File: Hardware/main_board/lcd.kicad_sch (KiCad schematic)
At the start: 0 parts

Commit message: sch: done LCD
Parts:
- added C66: 2.2uF, symbol Device:C
- added C67, C68, C69, C70: TBD, symbol Device:C
- added C71, C73, C74: TBD, symbol Device:C_Small
- added C72: 2.2uF, symbol Device:C_Small
- added C75: 100nF, symbol Device:C
- added C76: 100pF, symbol Device:C
- added J2: LCD, symbol Connector_Generic_MountingPin:Conn_01x30_MountingPin
- added J3: BACK_LIGHT, symbol Connector_Generic:Conn_01x02
- added R18: 0R, symbol Device:R_US
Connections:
- new net: C69.2, J2.24 (Pin_24)
- new net: C72.2, C73.1, J2.19 (Pin_19)
- new net: C73.2, J2.18 (Pin_18)
- new net: C67.2, J2.26 (Pin_26)
- new net: C68.2, J2.25 (Pin_25)
- new net: J3.1 (Pin_1), R18.1
- new net: C72.1, J2.20 (Pin_20)
- new net: C74.2, J2.17 (Pin_17)
- new net: C71.2, J2.21 (Pin_21)
- new net: C71.1, J2.22 (Pin_22)
- new net: C70.2, J2.23 (Pin_23)
- new net: C66.2, J2.27 (Pin_27)
- new net +3.3V: C75.2, C76.2, J2.10 (Pin_10), J2.11 (Pin_11), J2.12 (Pin_12), J2.15 (Pin_15), J2.5 (Pin_5), J2.6 (Pin_6), J2.7 (Pin_7), J2.8 (Pin_8), J2.9 (Pin_9)
- new net DISPLAY_CS: J2.2 (Pin_2)
- new net DISPLAY_DI: J2.4 (Pin_4)
- new net DISPLAY_RST: J2.3 (Pin_3)
- new net GND: C66.1, C67.1, C68.1, C69.1, C70.1, C74.1, C75.1, C76.1, J2.16 (Pin_16), J2.28 (Pin_28), J2.29 (Pin_29), J2.MP (MountPin)
- new net LCD_LED: J3.2 (Pin_2)
- new net SPI_D_MOSI: J2.14 (Pin_14)
- new net SPI_D_SCK: J2.13 (Pin_13)
- new net VSYS: R18.2
- no-connect marks 0 -> 2
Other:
- note added: "BACK LIGHT"
- note added: "LCD"
- note added: "VDD"

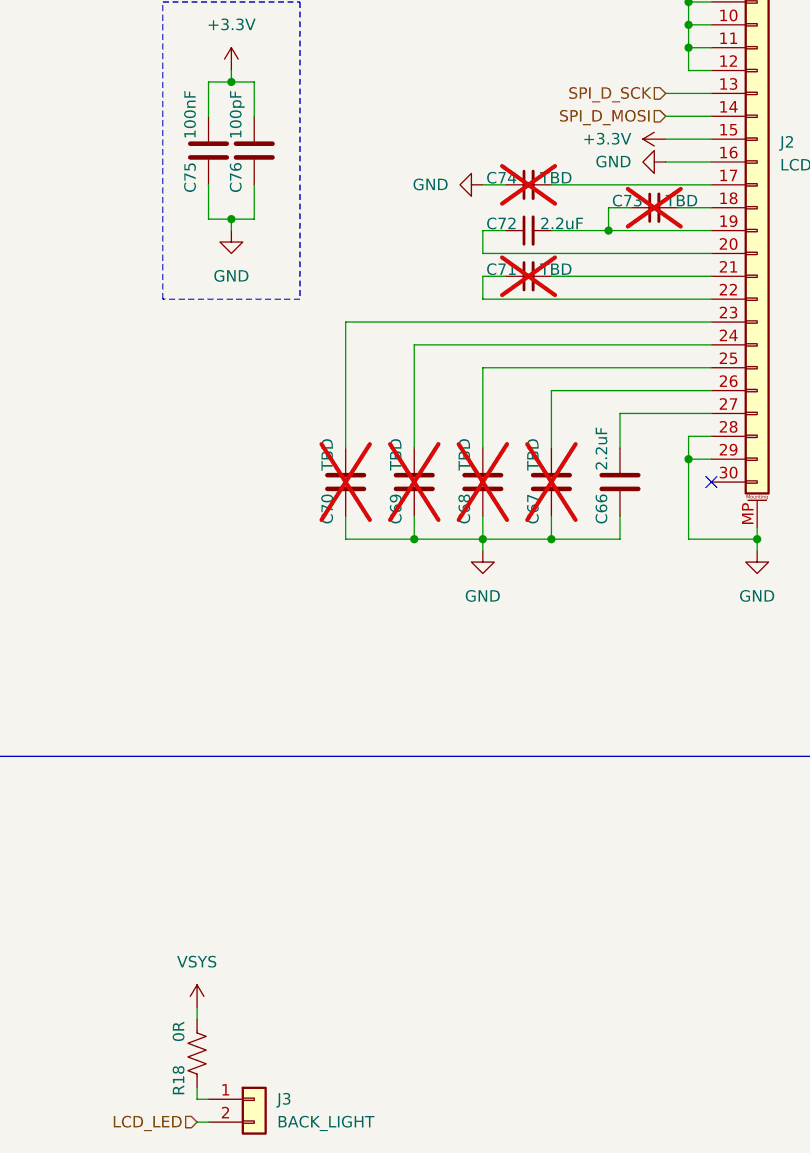
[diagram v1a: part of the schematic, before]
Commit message: sch: add some part of footprints
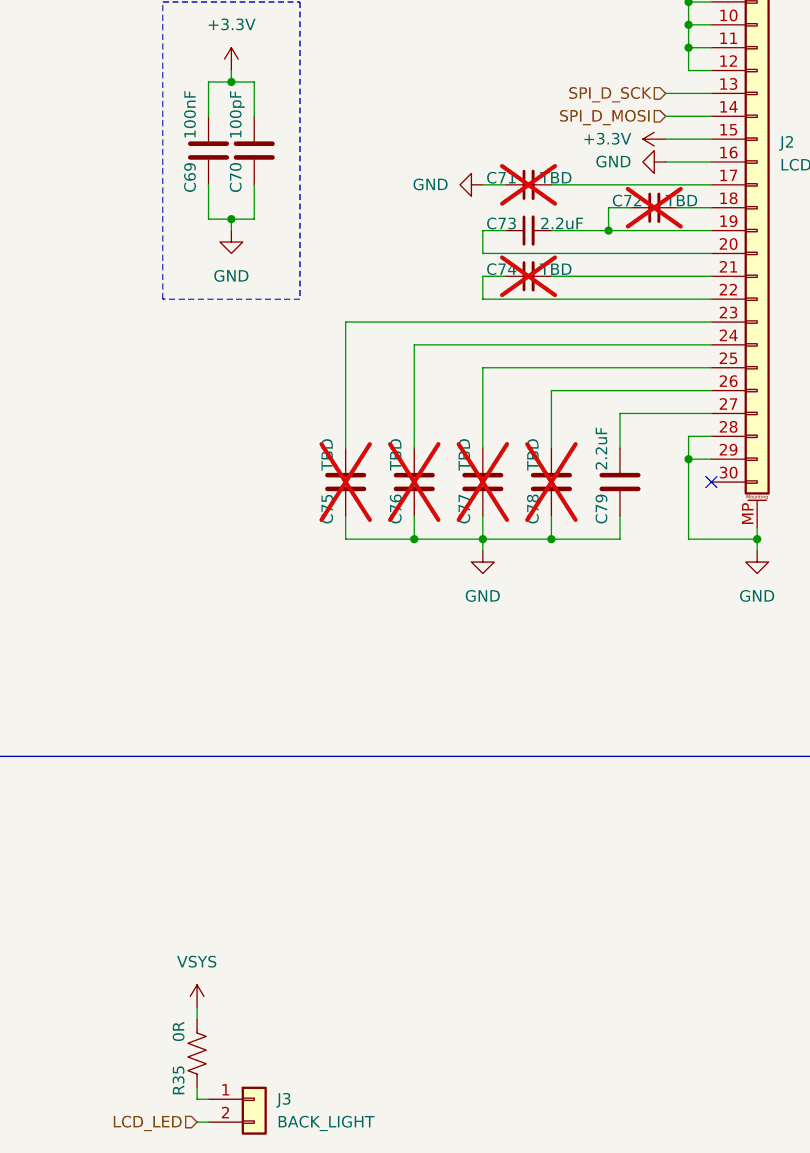
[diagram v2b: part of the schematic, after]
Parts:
- C69: renamed from C75; footprint (none) -> Capacitor_SMD:C_0402_1005Metric
- C70: renamed from C76; footprint (none) -> Capacitor_SMD:C_0402_1005Metric
- C71: renamed from C74; footprint (none) -> Capacitor_SMD:C_0402_1005Metric
- C72: renamed from C73; footprint (none) -> Capacitor_SMD:C_0402_1005Metric
- C73: renamed from C72; footprint (none) -> Capacitor_SMD:C_0402_1005Metric
- C74: renamed from C71; footprint (none) -> Capacitor_SMD:C_0402_1005Metric
- C75: renamed from C70; footprint (none) -> Capacitor_SMD:C_0402_1005Metric
- C76: renamed from C69; footprint (none) -> Capacitor_SMD:C_0402_1005Metric
- C77: renamed from C68; footprint (none) -> Capacitor_SMD:C_0402_1005Metric
- C78: renamed from C67; footprint (none) -> Capacitor_SMD:C_0402_1005Metric
- C79: renamed from C66; footprint (none) -> Capacitor_SMD:C_0402_1005Metric
- R35: renamed from R18; footprint (none) -> Resistor_SMD:R_0402_1005Metric
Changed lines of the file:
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@@
 		(on_board yes)
 		(dnp no)
-		(property "Reference" "C75"
+		(property "Reference" "C69"
 			(at 92.71 67.31 90)
 			(effects
@@
 			)
 		)
-		(property "Footprint" ""
+		(property "Footprint" "Capacitor_SMD:C_0402_1005Metric"
 			(at 93.0148 62.23 0)
 			(effects
@@
 			(project "main_board"
 				(path "/16216a68-6dea-41d7-8e15-2cc84f72f8e2/235dc31c-3814-4a70-a75b-2b905e486f6f"
-					(reference "C75")
+					(reference "C69")
 					(unit 1)
 				)
@@
 		(on_board yes)
 		(dnp yes)
-		(property "Reference" "C69"
+		(property "Reference" "C76"
 			(at 115.57 104.14 90)
 			(effects
@@
 			)
 		)
-		(property "Footprint" ""
+		(property "Footprint" "Capacitor_SMD:C_0402_1005Metric"
 			(at 115.8748 99.06 0)
 			(effects
@@
 			(project "main_board"
 				(path "/16216a68-6dea-41d7-8e15-2cc84f72f8e2/235dc31c-3814-4a70-a75b-2b905e486f6f"
-					(reference "C69")
+					(reference "C76")
 					(unit 1)
 				)
@@
 		(on_board yes)
 		(dnp yes)
-		(property "Reference" "C73"
+		(property "Reference" "C72"
 			(at 142.24 72.39 90)
 			(effects
@@
 			)
 		)
-		(property "Footprint" ""
+		(property "Footprint" "Capacitor_SMD:C_0402_1005Metric"
 			(at 143.51 72.39 0)
 			(effects
@@
 			(project "main_board"
 				(path "/16216a68-6dea-41d7-8e15-2cc84f72f8e2/235dc31c-3814-4a70-a75b-2b905e486f6f"
-					(reference "C73")
+					(reference "C72")
 					(unit 1)
 				)
@@
 		(on_board yes)
 		(dnp yes)
-		(property "Reference" "C67"
+		(property "Reference" "C78"
 			(at 130.81 104.14 90)
 			(effects
@@
 			)
 		)
-		(property "Footprint" ""
+		(property "Footprint" "Capacitor_SMD:C_0402_1005Metric"
 			(at 131.1148 99.06 0)
 			(effects
@@
 			(project "main_board"
 				(path "/16216a68-6dea-41d7-8e15-2cc84f72f8e2/235dc31c-3814-4a70-a75b-2b905e486f6f"
-					(reference "C67")
+					(reference "C78")
 					(unit 1)
 				)
@@
 		(on_board yes)
 		(dnp yes)
-		(property "Reference" "C68"
+		(property "Reference" "C77"
 			(at 123.19 104.14 90)
 			(effects
@@
 			)
 		)
-		(property "Footprint" ""
+		(property "Footprint" "Capacitor_SMD:C_0402_1005Metric"
 			(at 123.4948 99.06 0)
 			(effects
@@
 			(project "main_board"
 				(path "/16216a68-6dea-41d7-8e15-2cc84f72f8e2/235dc31c-3814-4a70-a75b-2b905e486f6f"
-					(reference "C68")
+					(reference "C77")
 					(unit 1)
 				)
@@
 		(dnp no)
 		(fields_autoplaced yes)
-		(property "Reference" "#PWR0108"
+		(property "Reference" "#PWR0115"
 			(at 96.52 81.28 0)
 			(effects
@@
 			(project "main_board"
 				(path "/16216a68-6dea-41d7-8e15-2cc84f72f8e2/235dc31c-3814-4a70-a75b-2b905e486f6f"
-					(reference "#PWR0108")
+					(reference "#PWR0115")
 					(unit 1)
 				)
@@
 		(on_board yes)
 		(dnp no)
-		(property "Reference" "R18"
+		(property "Reference" "R35"
 			(at 91.44 167.64 90)
 			(effects
@@
 			)
 		)
-		(property "Footprint" ""
+		(property "Footprint" "Resistor_SMD:R_0402_1005Metric"
 			(at 91.694 166.116 90)
 			(effects
@@
 			(project "main_board"
 				(path "/16216a68-6dea-41d7-8e15-2cc84f72f8e2/235dc31c-3814-4a70-a75b-2b905e486f6f"
-					(reference "R18")
+					(reference "R35")
 					(unit 1)
 				)
@@
 		(on_board yes)
 		(dnp no)
-		(property "Reference" "C72"
+		(property "Reference" "C73"
 			(at 128.27 74.93 90)
 			(effects
@@
 			)
 		)
-		(property "Footprint" ""
+		(property "Footprint" "Capacitor_SMD:C_0402_1005Metric"
 			(at 129.54 74.93 0)
 			(effects
@@
 			(project "main_board"
 				(path "/16216a68-6dea-41d7-8e15-2cc84f72f8e2/235dc31c-3814-4a70-a75b-2b905e486f6f"
-					(reference "C72")
+					(reference "C73")
 					(unit 1)
 				)
@@
 		(dnp no)
 		(fields_autoplaced yes)
-		(property "Reference" "#PWR0105"
+		(property "Reference" "#PWR0113"
 			(at 138.43 67.31 0)
 			(effects
@@
 			(project "main_board"
 				(path "/16216a68-6dea-41d7-8e15-2cc84f72f8e2/235dc31c-3814-4a70-a75b-2b905e486f6f"
-					(reference "#PWR0105")
+					(reference "#PWR0113")
 					(unit 1)
 				)
@@
 		(dnp no)
 		(fields_autoplaced yes)
-		(property "Reference" "#PWR0103"
+		(property "Reference" "#PWR0117"
 			(at 154.94 116.84 0)
 			(effects
@@
 			(project "main_board"
 				(path "/16216a68-6dea-41d7-8e15-2cc84f72f8e2/235dc31c-3814-4a70-a75b-2b905e486f6f"
-					(reference "#PWR0103")
+					(reference "#PWR0117")
 					(unit 1)
 				)
@@
 		(dnp no)
 		(fields_autoplaced yes)
-		(property "Reference" "#PWR0107"
+		(property "Reference" "#PWR0111"
 			(at 96.52 60.96 0)
 			(effects
@@
 			(project "main_board"
 				(path "/16216a68-6dea-41d7-8e15-2cc84f72f8e2/235dc31c-3814-4a70-a75b-2b905e486f6f"
-					(reference "#PWR0107")
+					(reference "#PWR0111")
 					(unit 1)
 				)
@@
 		(on_board yes)
 		(dnp yes)
-		(property "Reference" "C74"
+		(property "Reference" "C71"
 			(at 128.27 69.85 90)
 			(effects
@@
 			)
 		)
-		(property "Footprint" ""
+		(property "Footprint" "Capacitor_SMD:C_0402_1005Metric"
 			(at 129.54 69.85 0)
 			(effects
@@
 			(project "main_board"
 				(path "/16216a68-6dea-41d7-8e15-2cc84f72f8e2/235dc31c-3814-4a70-a75b-2b905e486f6f"
-					(reference "C74")
+					(reference "C71")
 					(unit 1)
 				)
@@
 		(dnp no)
 		(fields_autoplaced yes)
-		(property "Reference" "#PWR0104"
+		(property "Reference" "#PWR0114"
 			(at 118.11 69.85 0)
 			(effects
@@
 			(project "main_board"
 				(path "/16216a68-6dea-41d7-8e15-2cc84f72f8e2/235dc31c-3814-4a70-a75b-2b905e486f6f"
-					(reference "#PWR0104")
+					(reference "#PWR0114")
 					(unit 1)
 				)
@@
 		(dnp no)
 		(fields_autoplaced yes)
-		(property "Reference" "#PWR0109"
+		(property "Reference" "#PWR0110"
 			(at 148.59 39.37 0)
 			(effects
@@
 			(project "main_board"
 				(path "/16216a68-6dea-41d7-8e15-2cc84f72f8e2/235dc31c-3814-4a70-a75b-2b905e486f6f"
-					(reference "#PWR0109")
+					(reference "#PWR0110")
 					(unit 1)
 				)
@@
 		(dnp no)
 		(fields_autoplaced yes)
-		(property "Reference" "#PWR0110"
+		(property "Reference" "#PWR0118"
 			(at 92.71 165.1 0)
 			(effects
@@
 			(project "main_board"
 				(path "/16216a68-6dea-41d7-8e15-2cc84f72f8e2/235dc31c-3814-4a70-a75b-2b905e486f6f"
-					(reference "#PWR0110")
+					(reference "#PWR0118")
 					(unit 1)
 				)
@@
 		(on_board yes)
 		(dnp no)
-		(property "Reference" "C76"
+		(property "Reference" "C70"
 			(at 97.79 67.31 90)
 			(effects
@@
 			)
 		)
-		(property "Footprint" ""
+		(property "Footprint" "Capacitor_SMD:C_0402_1005Metric"
 			(at 98.0948 62.23 0)
 			(effects
@@
 			(project "main_board"
 				(path "/16216a68-6dea-41d7-8e15-2cc84f72f8e2/235dc31c-3814-4a70-a75b-2b905e486f6f"
-					(reference "C76")
+					(reference "C70")
 					(unit 1)
 				)
@@
 		(on_board yes)
 		(dnp yes)
-		(property "Reference" "C70"
+		(property "Reference" "C75"
 			(at 107.95 104.14 90)
 			(effects
@@
 			)
 		)
-		(property "Footprint" ""
+		(property "Footprint" "Capacitor_SMD:C_0402_1005Metric"
 			(at 108.2548 99.06 0)
 			(effects
@@
 			(project "main_board"
 				(path "/16216a68-6dea-41d7-8e15-2cc84f72f8e2/235dc31c-3814-4a70-a75b-2b905e486f6f"
-					(reference "C70")
+					(reference "C75")
 					(unit 1)
 				)
@@
 		(on_board yes)
 		(dnp no)
-		(property "Reference" "C66"
+		(property "Reference" "C79"
 			(at 138.43 104.14 90)
 			(effects
@@
 			)
 		)
-		(property "Footprint" ""
+		(property "Footprint" "Capacitor_SMD:C_0402_1005Metric"
 			(at 138.7348 99.06 0)
 			(effects
@@
 			(project "main_board"
 				(path "/16216a68-6dea-41d7-8e15-2cc84f72f8e2/235dc31c-3814-4a70-a75b-2b905e486f6f"
-					(reference "C66")
+					(reference "C79")
 					(unit 1)
 				)
@@
 		(dnp no)
 		(fields_autoplaced yes)
-		(property "Reference" "#PWR0102"
+		(property "Reference" "#PWR0116"
 			(at 124.46 116.84 0)
 			(effects
@@
 			(project ""
 				(path "/16216a68-6dea-41d7-8e15-2cc84f72f8e2/235dc31c-3814-4a70-a75b-2b905e486f6f"
-					(reference "#PWR0102")
+					(reference "#PWR0116")
 					(unit 1)
 				)
@@
 		(dnp no)
 		(fields_autoplaced yes)
-		(property "Reference" "#PWR0106"
+		(property "Reference" "#PWR0112"
 			(at 148.59 64.77 0)
 			(effects
@@
 			(project ""
 				(path "/16216a68-6dea-41d7-8e15-2cc84f72f8e2/235dc31c-3814-4a70-a75b-2b905e486f6f"
-					(reference "#PWR0106")
+					(reference "#PWR0112")
 					(unit 1)
 				)
@@
 		(on_board yes)
 		(dnp yes)
-		(property "Reference" "C71"
+		(property "Reference" "C74"
 			(at 128.27 80.01 90)
 			(effects
@@
 			)
 		)
-		(property "Footprint" ""
+		(property "Footprint" "Capacitor_SMD:C_0402_1005Metric"
 			(at 129.54 80.01 0)
 			(effects
@@
 			(project "main_board"
 				(path "/16216a68-6dea-41d7-8e15-2cc84f72f8e2/235dc31c-3814-4a70-a75b-2b905e486f6f"
-					(reference "C71")
-					(unit 1)
-				)
+					(reference "C74")
+					(unit 1)
+				)

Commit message: layout: change some of the footprint and start to layout
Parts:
- J2: footprint (none) -> Library:CONN30x1_FH34SRJ-30S-0.5SH50_HIR
- J3: footprint (none) -> LED_SMD:LED_1812_4532Metric
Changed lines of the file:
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@@
 			)
 		)
-		(property "Footprint" ""
+		(property "Footprint" "LED_SMD:LED_1812_4532Metric"
 			(at 99.06 171.45 0)
 			(effects
@@
 			)
 		)
-		(property "Footprint" ""
+		(property "Footprint" "Library:CONN30x1_FH34SRJ-30S-0.5SH50_HIR"
 			(at 154.94 64.77 0)
 			(effects

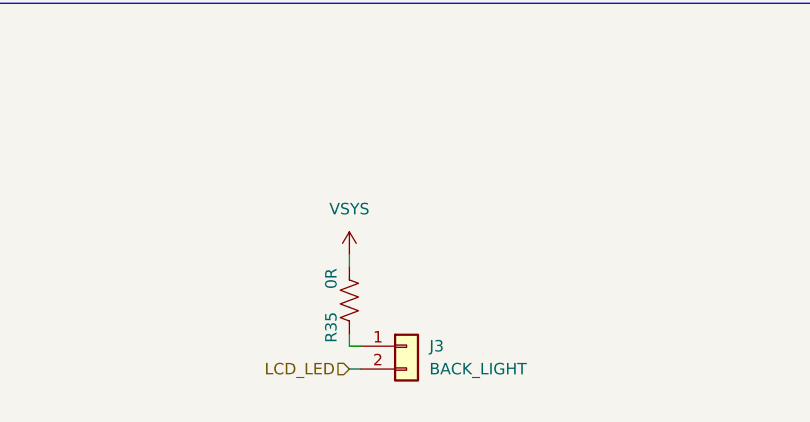
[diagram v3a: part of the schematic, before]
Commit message: layout: place the led driver
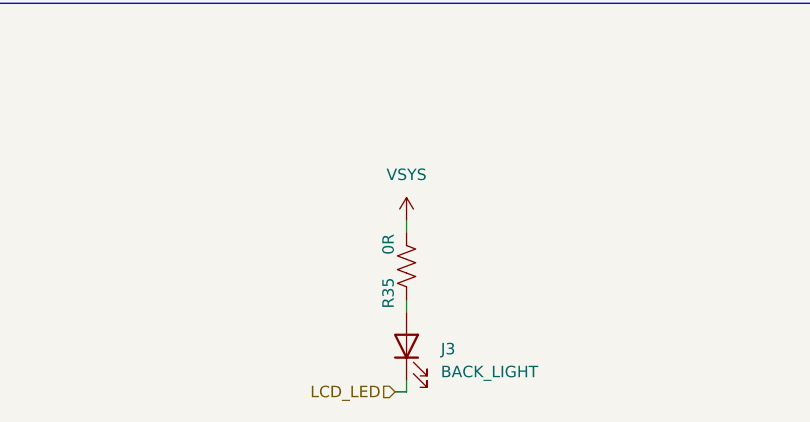
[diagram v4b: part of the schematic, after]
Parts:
- J3: footprint LED_SMD:LED_1812_4532Metric -> Library:ERC12864FAMF03; symbol Connector_Generic:Conn_01x02 -> Device:LED
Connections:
- net LCD_LED: now also J3.1 (K); no longer J3.2 (Pin_2)
- net at R35.1: now also J3.2 (A); no longer J3.1 (Pin_1)
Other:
- moved on the sheet: R35
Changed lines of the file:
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@@
 	(wire
 		(pts
-			(xy 92.71 161.29) (xy 92.71 162.56)
+			(xy 99.06 157.48) (xy 99.06 158.75)
 		)
 		(stroke
@@
 	(wire
 		(pts
-			(xy 93.98 171.45) (xy 92.71 171.45)
-		)
-		(stroke
-			(width 0)
-			(type default)
-		)
-	)
-	(wire
-		(pts
 			(xy 109.22 99.06) (xy 109.22 85.09)
 		)
@@
 	(wire
 		(pts
-			(xy 92.71 170.18) (xy 92.71 171.45)
-		)
-		(stroke
-			(width 0)
-			(type default)
-		)
-	)
-	(wire
-		(pts
 			(xy 132.08 69.85) (xy 149.86 69.85)
 		)
@@
 	(wire
 		(pts
+			(xy 99.06 175.26) (xy 99.06 176.53)
+		)
+		(stroke
+			(width 0)
+			(type default)
+		)
+	)
+	(wire
+		(pts
 			(xy 149.86 97.79) (xy 147.32 97.79)
 		)
@@
 	(wire
 		(pts
+			(xy 99.06 166.37) (xy 99.06 167.64)
+		)
+		(stroke
+			(width 0)
+			(type default)
+		)
+	)
+	(wire
+		(pts
 			(xy 139.7 106.68) (xy 139.7 109.22)
 		)
@@
 	(wire
 		(pts
-			(xy 92.71 173.99) (xy 93.98 173.99)
+			(xy 97.79 176.53) (xy 99.06 176.53)
 		)
 		(stroke
@@
 	(hierarchical_label "LCD_LED"
 		(shape input)
-		(at 92.71 173.99 180)
+		(at 97.79 176.53 180)
 		(fields_autoplaced yes)
 		(effects
@@
 	)
 	(symbol
-		(lib_id "Connector_Generic:Conn_01x02")
-		(at 99.06 171.45 0)
+		(lib_id "Device:LED")
+		(at 99.06 171.45 90)
 		(unit 1)
 		(exclude_from_sim no)
@@
 		(fields_autoplaced yes)
 		(property "Reference" "J3"
-			(at 101.6 171.4499 0)
-			(effects
-				(font
-					(size 1.27 1.27)
-				)
-				(justify left)
+			(at 102.87 171.7674 90)
+			(effects
+				(font
+					(size 1.27 1.27)
+				)
+				(justify right)
 			)
 		)
 		(property "Value" "BACK_LIGHT"
-			(at 101.6 173.9899 0)
-			(effects
-				(font
-					(size 1.27 1.27)
-				)
-				(justify left)
-			)
-		)
-		(property "Footprint" "LED_SMD:LED_1812_4532Metric"
+			(at 102.87 174.3074 90)
+			(effects
+				(font
+					(size 1.27 1.27)
+				)
+				(justify right)
+			)
+		)
+		(property "Footprint" "Library:ERC12864FAMF03"
 			(at 99.06 171.45 0)
 			(effects
@@
 			)
 		)
-		(property "Description" "Generic connector, single row, 01x02, script generated (kicad-library-utils/schlib/autogen/connector/)"
+		(property "Description" "Light emitting diode"
 			(at 99.06 171.45 0)
 			(effects
@@
 	(symbol
 		(lib_id "Device:R_US")
-		(at 92.71 166.37 180)
+		(at 99.06 162.56 180)
 		(unit 1)
 		(exclude_from_sim no)
@@
 		(dnp no)
 		(property "Reference" "R35"
-			(at 91.44 167.64 90)
+			(at 97.79 163.83 90)
 			(effects
 				(font
@@
 		)
 		(property "Value" "0R"
-			(at 91.44 165.1 90)
+			(at 97.79 161.29 90)
 			(effects
 				(font
@@
 		)
 		(property "Footprint" "Resistor_SMD:R_0402_1005Metric"
-			(at 91.694 166.116 90)
+			(at 98.044 162.306 90)
 			(effects
 				(font
@@
 		)
 		(property "Datasheet" "~"
-			(at 92.71 166.37 0)
+			(at 99.06 162.56 0)
 			(effects
 				(font
@@
 		)
 		(property "Description" "Resistor, US symbol"
-			(at 92.71 166.37 0)
+			(at 99.06 162.56 0)
 			(effects
 				(font
@@
 	(symbol
 		(lib_id "power:+3.3V")
-		(at 92.71 161.29 0)
+		(at 99.06 157.48 0)
 		(unit 1)
 		(exclude_from_sim no)
@@
 		(fields_autoplaced yes)
 		(property "Reference" "#PWR0118"
-			(at 92.71 165.1 0)
+			(at 99.06 161.29 0)
 			(effects
 				(font
@@
 		)
 		(property "Value" "VSYS"
-			(at 92.71 156.21 0)
+			(at 99.06 152.4 0)
 			(effects
 				(font
@@
 		)
 		(property "Footprint" ""
-			(at 92.71 161.29 0)
+			(at 99.06 157.48 0)
 			(effects
 				(font
@@
 		)
 		(property "Datasheet" ""
-			(at 92.71 161.29 0)
+			(at 99.06 157.48 0)
 			(effects
 				(font
@@
 		)
 		(property "Description" "Power symbol creates a global label with name \"+3.3V\""
-			(at 92.71 161.29 0)
-			(effects
-				(font
+			(at 99.06 157.48 0)
+			(effects
+				(font
